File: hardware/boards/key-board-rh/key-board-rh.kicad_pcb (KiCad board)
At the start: 2 copper layers, 106.1 x 42 mm, 38 parts, among them J1 12-way, SW1 KS-33, SW2 KS-33, SW3 KS-33, SW4 KS-33, SW5 KS-33, SW6 KS-33, U1 74HCS165

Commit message: Fit C-BULK-CHAIN on both key boards instead of leaving it empty
The 10uF reservoir on each key board's 3V3 (C7 on the left-hand board,
C8 on the right) was a do-not-fit footprint, to be fitted at bring-up
only if the rail rang. It costs cents, so it is now a fitted,
machine-placed part (owner, 2026-09-28): Samsung CL21A106KAYNNNE, LCSC
C15850, a JLC Basic part.

The key-chain simulation now calls the fitted board "as ordered":
- rail-as-ordered: 5 mV peak to peak on the key board's 3V3.
- rail-impedance-as-ordered: a 2.2 ohm peak.
- The new rail-without-bulk holds the same limits with it left off
  (72 mV). A board built without the part still works; the part makes
  the rail quieter.
- rail-impedance-without-bulk (176-217 ohm peak) replaces
  rail-impedance-with-bulk; edge-droop-as-ordered is renamed
  edge-droop-decoupler-alone, since it models the decoupler with the
  bulk capacitor off.
Both boards' own simulations now include the part.

The sheets, the BOM row, the loom page, cluster-boards.md and both
board READMEs no longer treat it as optional. Both boards are re-laid
out (no DNP mark), checked at 0 errors and re-rendered, and the part
is in each board's JLC BOM and CPL.

Co-Authored-By: Claude Opus 5.5 <noreply@anthropic.com>
Claude-Session: https://claude.ai/code/session_01LmB4muFXnoLprWX4JzuJ5A
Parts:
- C8: value 10uF DNP -> 10uF
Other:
- board text added: "C8"
- board text removed: "C8 DNP"

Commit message: Hang the key boards on PEM studs pressed flush into the plate
The owner asked for the key-board fasteners to be flush with the key
plate. A countersunk M2 head is as tall as the 1.20 mm plate is thick,
which would leave a knife-edge hole. So each corner now takes a PEM FHL
self-clinching flush-head stud pressed into the plate (owner:
"convert to that"). The rest of the stack is below the plate: spacer,
washer, the board, and a nut underneath. Nothing stands above the plate,
so the wood top has no pockets and there is no epoxy: the clinch keeps
each stud from turning, and the nuts still come off from below.

- M2.5: PEM's bulletin has no M2 flush-head stud. FHL rather than FH
  because PEM publishes FHL data in 1.2 mm aluminium (push-out 285 N,
  torque-out 0.55 N.m, nut torque 0.32 N.m) and it needs 2.8 mm to an
  edge. The model puts every stud 5.1 mm from the nearest cutout, where
  FH would need 5.4. Zinc-plated steel, per PEM's galvanic guidance.
  The bulletin and the finish guide are banked (R17).
- Spacer: no stocked M2.5 spacer is 1.8 mm, and 1.5 or 2.0 puts the
  board at the edge of the switch pins' window. Ettinger 005.52.023
  (2.0 mm) is faced down to 1.8 (banked, R18). The Wurth WA-SMST
  spacers carry a reflow spigot under the body, so the M2 one the old
  stack named was never a plain 2 mm spacer.
- body.yaml: kb_stud_* replace kb_screw_*, kb_pocket_* and
  kb_plate_hole. The washer and nut go to M2.5, and kb_mount_inset is
  now set by the nut's keep-out (3.6).
- New checks: stud edge distance, thread past the nut at the shortest
  stud, unthreaded shank inside the spacer, and the least tail margin
  (6.65 against the 10.1 kept). 0 clashes. The oak-pockets DXF is
  gone.
- Both key boards re-laid with M2.5 holes and keep-outs: 0 errors
  each, renders and fab regenerated.
- BOM: MECH-KB-STUD replaces MECH-KB-SCREW, the spacer, washer and nut
  rows go to M2.5, and ADH-EPOXY is removed.
- ADR 0020 Amendment 4 records the change. ADR 0009, cluster-boa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
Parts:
- H1, H2, H3, H4: value M2 mount -> mount; footprint MountingHole:MountingHole_2.2mm_M2 -> MountingHole:MountingHole_2.7mm_M2.5
- moved H1 0.28 mm to (208.8, 138.9)
- moved H2 0.28 mm to (208.8, 104.1)
- moved H3 0.28 mm to (307.7, 138.9)
- moved H4 0.28 mm to (307.7, 104.1)

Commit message: etherCON: PCB-mounted NE8FAV on an adapter, soldered to a main-board tongue (ADR 0021)
The instrument's etherCON becomes a Neutrik NE8FAV (A-series, vertical PCB,
rear mounting), soldered to a small adapter board behind the tail cap. J-UMB
becomes a 1 x 8 2.54 mm right-angle header soldered into the adapter and a
new tongue of the main board, so the umbilical has no cable and no mated
contact inside the body; CBL-UMB-PATCH is gone. Mounting the NE8FAH on the
main board directly would put its body 3 mm above the oak top's underside,
so the vertical part on an adapter it is. Latch up: the square flange
retires ADR 0009's rotation. The tail cap gets a recess from outside that
leaves the NE8FAV its 3 mm maximum panel.

- datasheets: NE8FAH, NE8FAH-C5 and NE8FAV drawings, data sheets and 3D
  models banked (fragment R23), with a BLOCKED row for the non-existent
  NE8FAH-C5E/-C6.
- config/body.yaml ethercon: NE8FAV numbers with sources; boards.umb_joint_*
  and umb_adapter_t; patch lead, rear socket and old J-UMB envelopes removed.
- CAD: the connector, adapter, J-UMB and tongue modelled; new DRC rules
  (adapter behind the Matrix, J-UMB under it, J-UMB's row clear of the
  footprint, the recess inside the face, the PUSH tab). 0 clashes.
- The patch plug no longer sets the tail: the body shortens by 1.9 mm, the
  hand gap drops to its minimum and the right hand moves 0.2 mm toward the
  mouth; the LH ribbon hairpin's clearance to the middle lid screw moved
  J-CHAIN LH 0.5 mm. Both key boards re-laid out from the body CAD (0
  errors each), renders and fab/ regenerated.
- BOM: J-UMBILICAL is the module end only; J-UMBILICAL-INST, PCB-UMB-ADAPTER
  and MECH-ETHERCON-SCREW added; J-UMB, PCB-CARRIER, ENDCAP-TAIL and the
  cable shell row updated (the NE8FAV does not name the NE8MX).
- spi-link netlist and circuit.yaml, carrier.md, spi-link.md, DESIGN.md,
  hardware/README.md, the register's body-thickness derivation, and pointers
  in ADRs 0001, 0004, 0009 and 0017. ADR inde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
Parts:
- moved H1 0.20 mm to (208.6, 138.9)
- moved H2 0.20 mm to (208.6, 104.1)
- moved J1 0.20 mm to (231.6, 111.2)
- moved C1 0.20 mm to (225.3, 121.5)
- moved C2 0.20 mm to (245.3, 121.5)
- moved C3 0.20 mm to (265.3, 121.5)
- moved C4 0.20 mm to (283.3, 130.5)
- moved C5 0.20 mm to (283.3, 112.5)
- moved C6 0.20 mm to (301.3, 130.5)
- moved C7 0.20 mm to (252.0, 108.2)
- moved C8 0.20 mm to (227.5, 108.0)
- moved H3 0.20 mm to (307.5, 138.9)
- moved H4 0.20 mm to (307.5, 104.1)
- moved R1 0.20 mm to (228.0, 124.2)
- moved R10 0.20 mm to (286.0, 109.8)
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
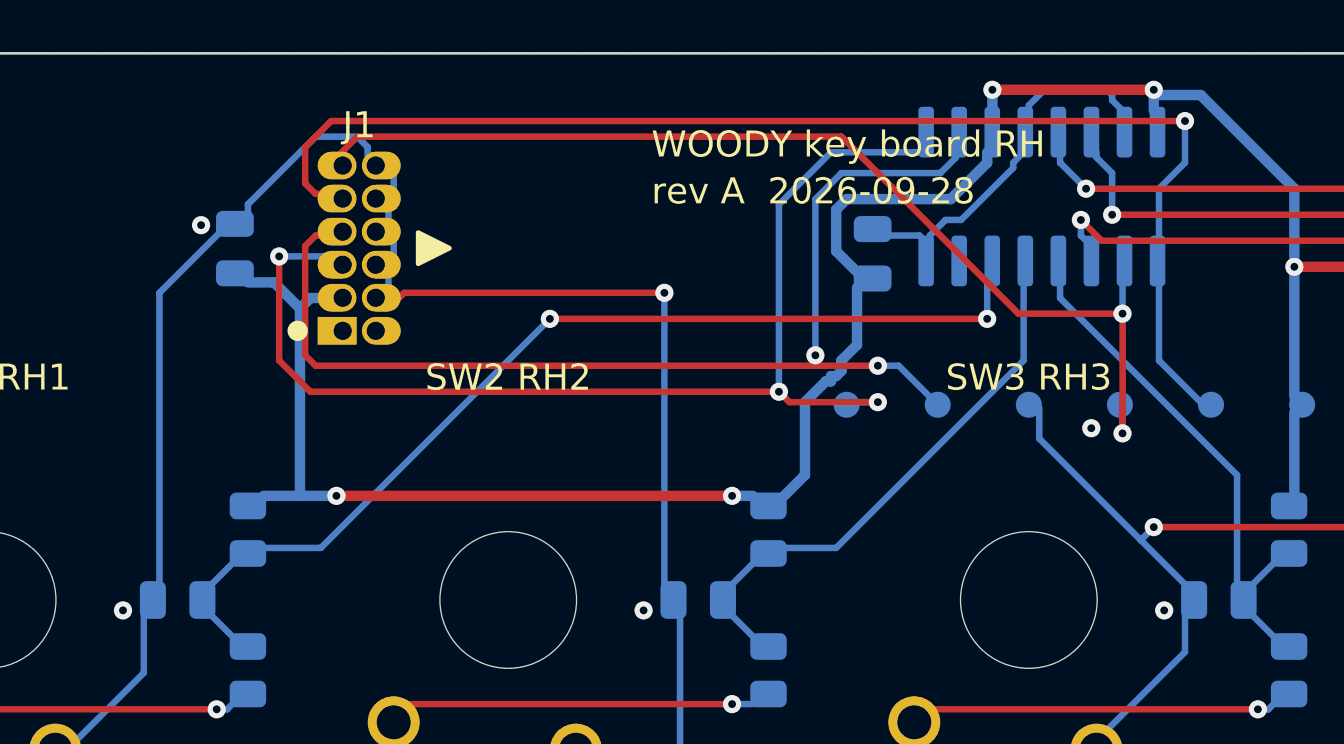
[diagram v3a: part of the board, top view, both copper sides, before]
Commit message: Main board: apply the chosen parts to every symbol and row
Every main-board and adapter symbol now carries Footprint, Manufacturer,
MPN, LCSC and Assembly. The values come from the selections whose
datasheets are banked. The BOM rows follow those choices:

- D-USBOR is the SS14 (SMA).
- J-LED is four solder pads, not a connector.
- L-BUCK-IN is 22 uH, C-BUCK-IN is a UCM electrolytic, C-STRIP-BULK is
  470 uF 25 V.
- D-TVS-BREATH is the PESD12VS1UA (SOD-323); the UB is SOD523.
- J-UMB is the hanxia header. Its posts go through the adapter and its
  tails through the tongue; the old wording had them swapped.
- U-BUCK and U-BREATH say where to buy.
- C-ADC-BULK is 1206 if fitted.

The body and geometry follow the chosen parts:

- The J-UMB and J-MCU envelopes in config/body.yaml are now read off the
  parts' drawings.
- J-MCU is longer, so the regulator block moved and the right-hand ribbon
  header followed it by 1.5 mm. The RH key board is re-laid out, with C8
  moving with the header's 3V3 pin. It checks clean.
- A mount candidate is now nudged by up to 3 mm before it is dropped. All
  seven main-board mounts hold.

New footprints and pages:

- New woody.pretty footprints: the MPXV4006DP (case 1351-01) from
  breath-sense-link.md's land pattern, and the NE8FAV from Neutrik's
  layout, mirrored to the top view.
- The input-LC derivation uses the chosen capacitor's banked ESR: Q is at
  most 1.8, and the margin is 120x worst case.
- The main-board README lists what is still open before layout.

Co-Authored-By: Claude Opus 5.5 <noreply@anthropic.com>
Claude-Session: https://claude.ai/code/session_01LmB4muFXnoLprWX4JzuJ5A
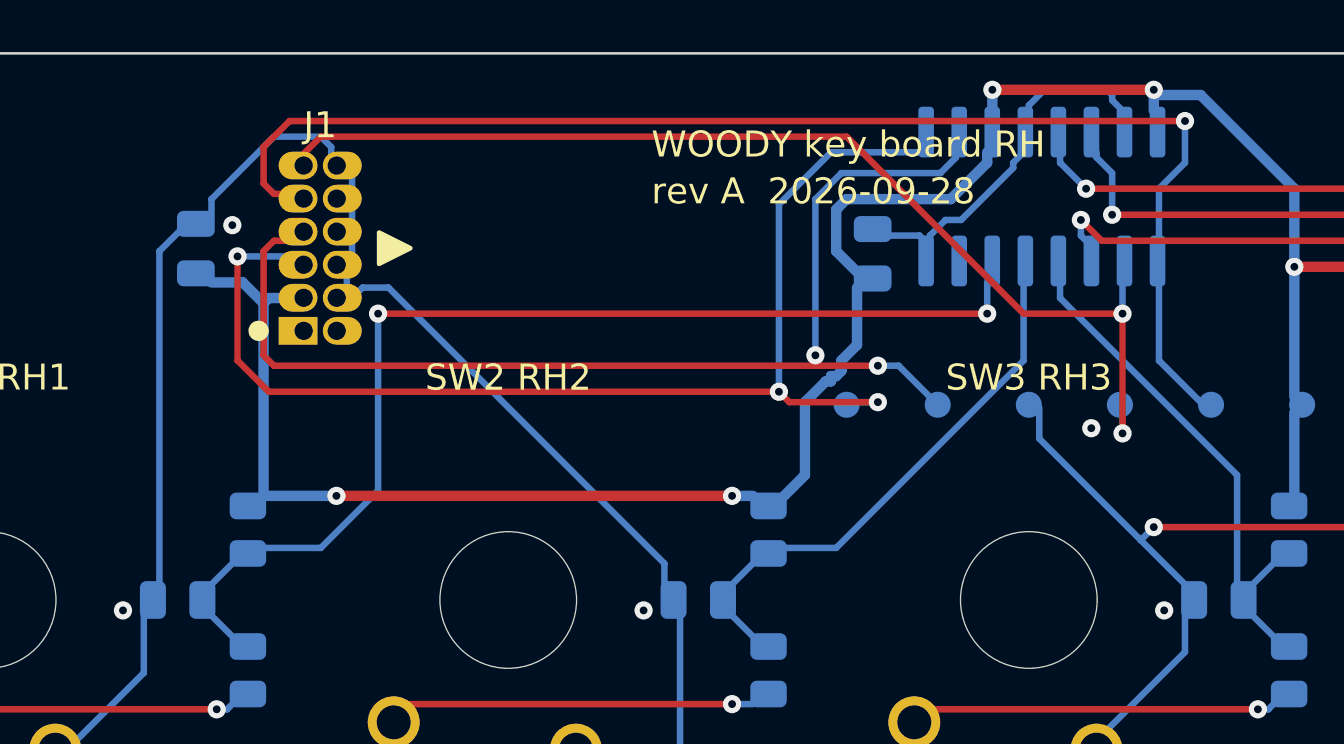
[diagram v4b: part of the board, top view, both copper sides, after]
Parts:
- moved C8 1.50 mm to (226.0, 108.0)
- moved J1 1.50 mm to (230.1, 111.2)
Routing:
- net GND_CHAIN: track 174.5 -> 169.6 mm, vias 10 -> 9
- net /KEY_RH1: track 35.1 -> 39.0 mm
- net /CHAIN_SHLD: track 46.7 -> 48.5 mm
- net /HOP_RH_RT: track 43.9 -> 45.5 mm
- net /HOP_LT_RH: track 42.3 -> 43.9 mm
- net /CHAIN_SCK: track 39.9 -> 41.3 mm

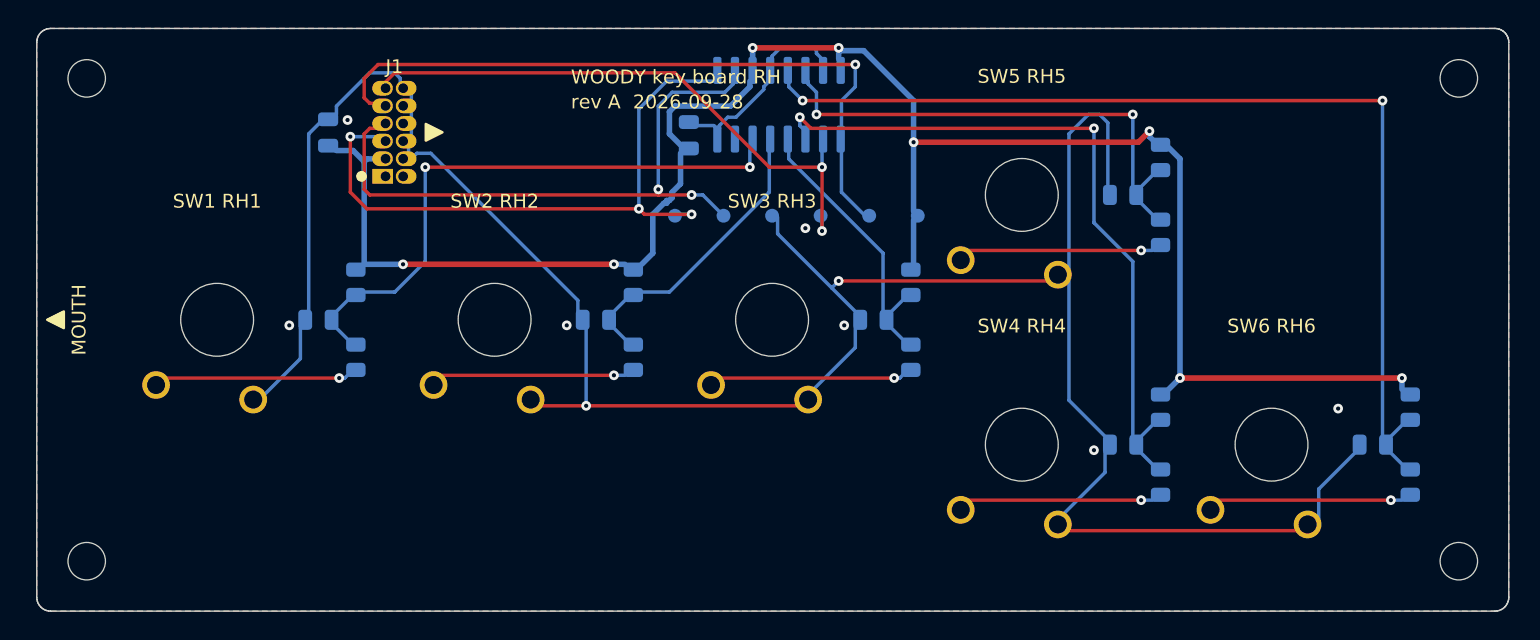
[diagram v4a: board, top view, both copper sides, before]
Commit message: Main board: in the U-bolt's clamp, mounted under the key boards' mounts
The owner: no big holes and no narrowing of the main board at the U-bolt,
and the key boards' standoff locations carried down to the main board, with
a pair at each end (ADR 0022 points 7 and 8).

- The U-bolt's nuts now stand on the board's top face: backplate, DIN 433
  washer, board, washer, nyloc. The board has a 4 mm hole per leg; the
  lid-screw notches are a clearance hole opened to the edge. The station
  goes from one 10.6 mm neck to 24.4 mm of board (drc.echo).
- Twelve mounts: one under each of the key boards' eight (the mouth-end
  column in each hand 0.5 mm toward the mouth, clear of a thumb cutout,
  the thumb plate reaching round its stud), a pair at the mouth and a pair
  on the tongue before J-UMB. BOM counts follow: 4 plate, 8 oak.
- Backplate 16 mm along the body (hardware.backplate_l), clear of the
  column spacers either side. New MECH-UBOLT-WASHER row. The U-bolt legs
  are exported to pcb-geometry.echo for the main board's layout.
- RH key board re-laid out at 1.6 mm: every net routes on the first pass,
  one passive pattern on all six keys, pcb.py check 0 errors. kicad.py
  check passes on all four boards.

Co-Authored-By: Claude Opus 5.5 <noreply@anthropic.com>
Claude-Session: https://claude.ai/code/session_01LmB4muFXnoLprWX4JzuJ5A
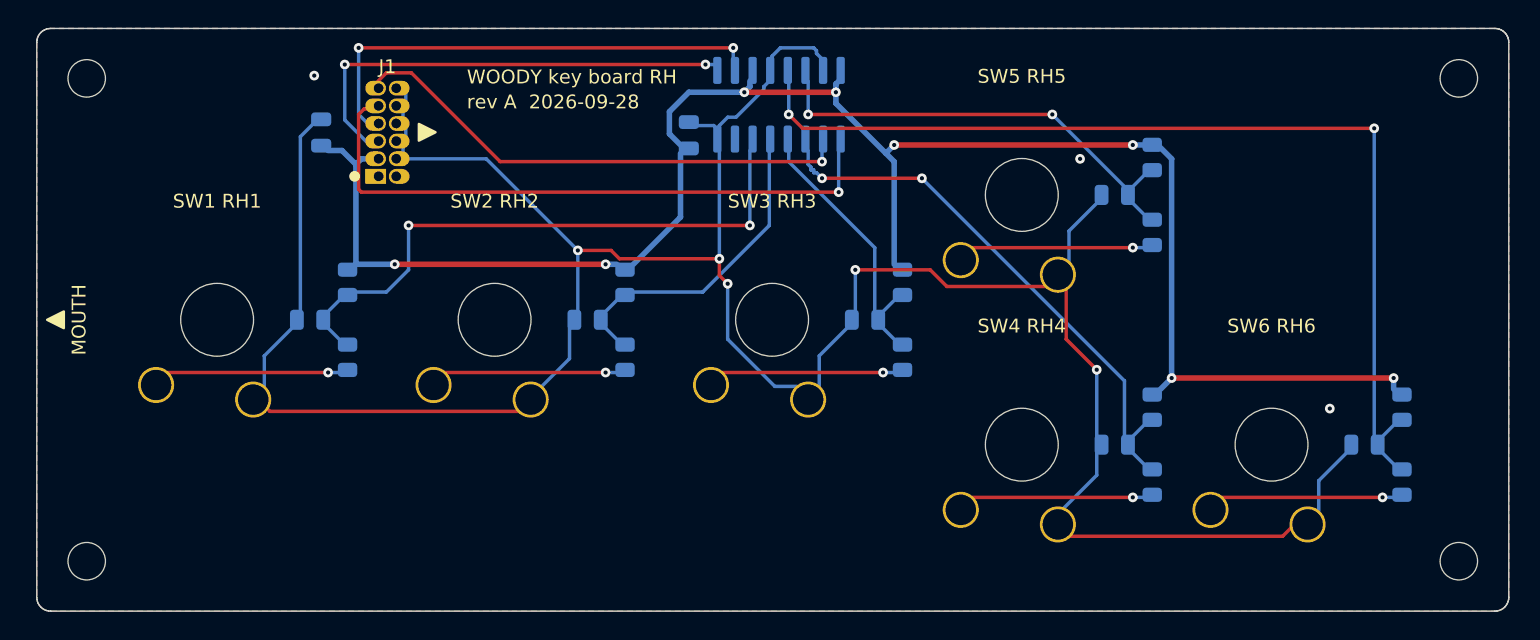
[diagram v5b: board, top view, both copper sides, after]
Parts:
- removed TP1, TP2, TP3, TP4, TP5, TP6: test pad, TestPoint:TestPoint_Pad_D1.0mm
- moved R5 0.60 mm to (267.4, 124.2)
- moved R6 0.60 mm to (267.4, 118.8)
- moved C1 0.60 mm to (224.7, 121.5)
- moved C2 0.60 mm to (244.7, 121.5)
- moved C3 0.60 mm to (264.7, 121.5)
- moved C4 0.60 mm to (282.7, 130.5)
- moved C5 0.60 mm to (282.7, 112.5)
- moved C6 0.60 mm to (300.7, 130.5)
- moved R10 0.60 mm to (285.4, 109.8)
- moved R11 0.60 mm to (303.4, 133.2)
- moved R12 0.60 mm to (303.4, 127.8)
- moved R7 0.60 mm to (285.4, 133.2)
- moved R8 0.60 mm to (285.4, 127.8)
- moved R9 0.60 mm to (285.4, 115.2)
- moved R1 0.60 mm to (227.4, 124.2)
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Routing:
- net /HOP_RH_RT: track 45.5 -> 33.1 mm, vias 3 -> 2
- net /KEY_RH4: track 48.0 -> 36.8 mm
- net /HOP_LT_RH: track 43.9 -> 33.4 mm
- net /CHAIN_SCK: track 41.3 -> 36.0 mm, vias 2 -> 1
- net /CHAIN_SHLD: track 48.5 -> 43.8 mm
- net V3V3_CHAIN_RH: track 127.3 -> 123.8 mm
- net /KEY_RH5: track 32.9 -> 29.6 mm
- net /KEY_RH2: track 17.4 -> 19.5 mm
- net GND_CHAIN: track 169.6 -> 170.8 mm, vias 9 -> 8
- net /KEY_RH1: track 39.0 -> 39.9 mm
- net /RH2/SWITCH_LEG: track 13.2 -> 12.4 mm
- net /RH6/SWITCH_LEG: track 13.2 -> 12.4 mm
- net /RH5/SWITCH_LEG: track 13.2 -> 12.4 mm
- net /RH4/SWITCH_LEG: track 13.2 -> 12.4 mm
- net /RH1/SWITCH_LEG: track 13.1 -> 12.4 mm
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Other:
- board text removed: "TP1"
- board text removed: "TP1 QH TP2 SER TP3 GND"
- board text removed: "TP2"
- board text removed: "TP3"
- board text removed: "TP4"
- board text removed: "TP4 SCK TP5 SH/LD TP6 3V3"
- board text removed: "TP5"
- board text removed: "TP6"

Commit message: WIP: the cassette - drop-in internals on columns, no body fasteners (ADR 0024)
Checkpoint of work in progress: model, config, BOM fragments, key-board
re-layouts, ADR 0024 and amendments. Clash check and gates still to run.

Co-Authored-By: Claude Opus 5.5 <noreply@anthropic.com>
Claude-Session: https://claude.ai/code/session_01LmB4muFXnoLprWX4JzuJ5A
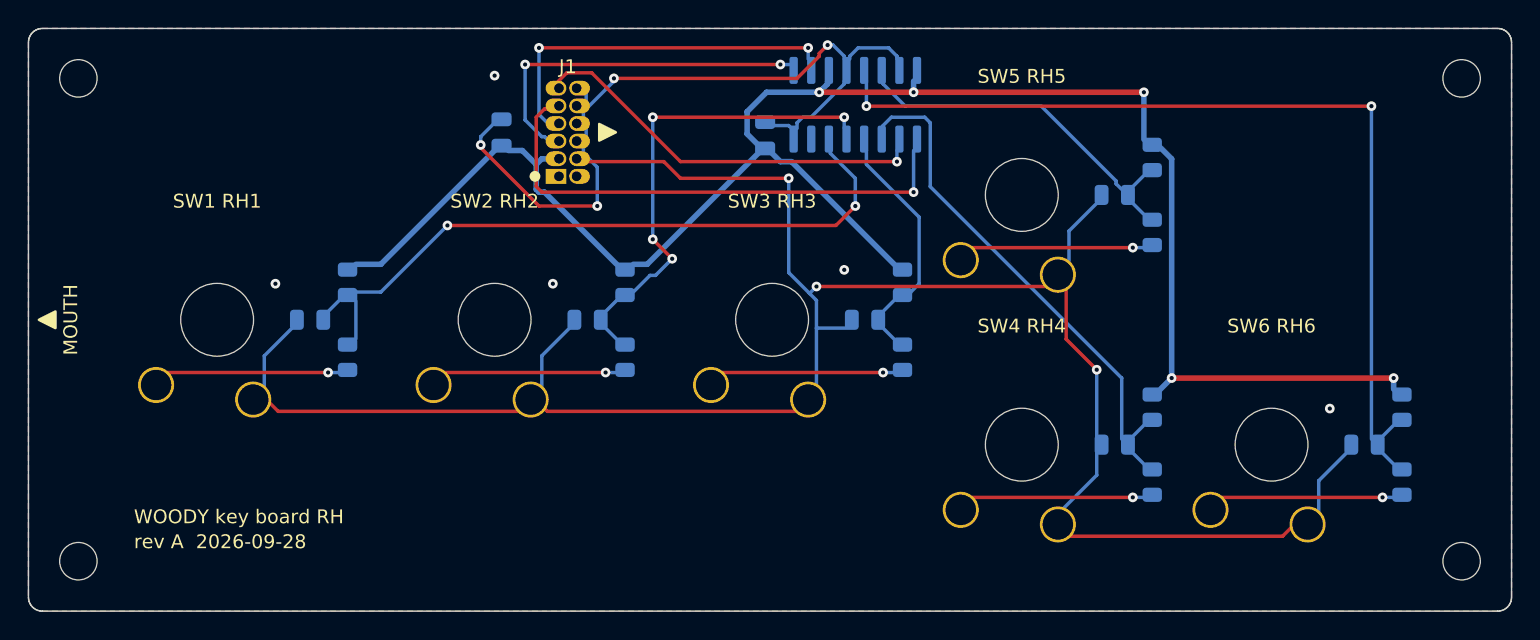
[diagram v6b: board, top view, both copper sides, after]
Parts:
- moved C8 13.0 mm to (238.5, 108.0)
- moved J1 13.0 mm to (242.6, 111.2)
- moved C7 5.50 mm to (257.5, 108.2)
- moved U1 5.50 mm to (264.0, 106.0)
- moved H1 0.60 mm to (208.0, 138.9)
- moved H2 0.60 mm to (208.0, 104.1)
- moved H3 0.20 mm to (307.7, 138.9)
- moved H4 0.20 mm to (307.7, 104.1)
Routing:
- net GND_CHAIN: track 170.8 -> 189.8 mm, vias 8 -> 12
- net /KEY_RH2: track 19.5 -> 31.4 mm, vias 0 -> 4
- net /HOP_RH_RT: track 33.1 -> 25.4 mm
- net /CHAIN_SCK: track 36.0 -> 28.4 mm
- net /HOP_LT_RH: track 33.4 -> 25.8 mm
- net /CHAIN_SHLD: track 43.8 -> 36.4 mm
- net /KEY_RH1: track 39.9 -> 47.2 mm
- net /KEY_RH5: track 29.6 -> 22.9 mm, vias 2 -> 0
- net /KEY_RH6: track 69.5 -> 64.5 mm
- net /KEY_RH3: track 16.4 -> 14.3 mm
- net /KEY_RH4: track 36.8 -> 34.8 mm, vias 2 -> 0
- net V3V3_CHAIN_RH: track 123.8 -> 123.2 mm, vias 8 -> 5
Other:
- board size 106.1 x 42 mm -> 106.9 x 42 mm
